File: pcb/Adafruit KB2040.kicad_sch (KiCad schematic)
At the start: 12 parts, among them M1 Vibrating-Motor, SW1 SW_SPST, U1 kb2040, U2 2465

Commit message: I messed around with the wiring more - now it should be done. need to do some final checks before sent off (whatever that means)
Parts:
- removed M1: Vibrating-Motor, Connector_PinHeader_2.54mm:PinHeader_1x02_P2.54mm_Vertical, symbol Motor:Motor_DC
- removed SW1: SW_SPST, Connector_PinHeader_2.54mm:PinHeader_1x02_P2.54mm_Vertical, symbol Switch:SW_SPST
- added ENPOINT1, GNDPOINT1: TestPoint_Small, TestPoint:TestPoint_Pad_2.0x2.0mm, symbol Connector:TestPoint_Small
- OLED1: footprint Connector_PinHeader_2.00mm:PinHeader_1x04_P2.00mm_Horizontal -> Connector_PinHeader_2.00mm:PinHeader_1x04_P2.00mm_Vertical
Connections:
- net D10ASSY: now also D-Pad1.4 (Center), U1.26 (D10); no longer D-Pad1.1 (Up), U1.10 (D6)
- net EN: now also ENPOINT1.1
- net GND: now also GNDPOINT1.1
- net at U1.9 (D5): no longer D-Pad1.4 (Center)
- new net D6ASSY: D-Pad1.1 (Up), U1.10 (D6)

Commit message: Maybe finished the board? looks good to me. gonna look it over with others first
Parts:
- added C2, C3, C4: 0.1uF, Capacitor_SMD:C_0201_0603Metric_Pad0.64x0.40mm_HandSolder, symbol Device:C_Small
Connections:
- net +3.3V: now also C2.1; no longer OLED1.2 (VCC)
- net +5V: now also C4.1
- net GND: now also C2.2, C4.2; no longer OLED1.1 (GND)

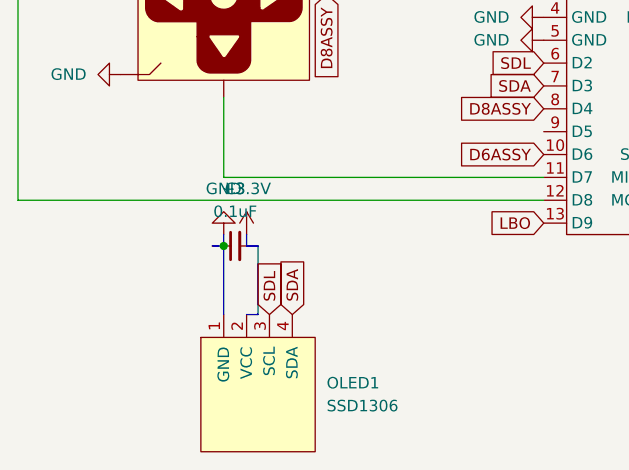
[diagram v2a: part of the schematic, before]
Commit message: Refreshed th eoled design to accomodate the screen i found - swapped vcc and gnd
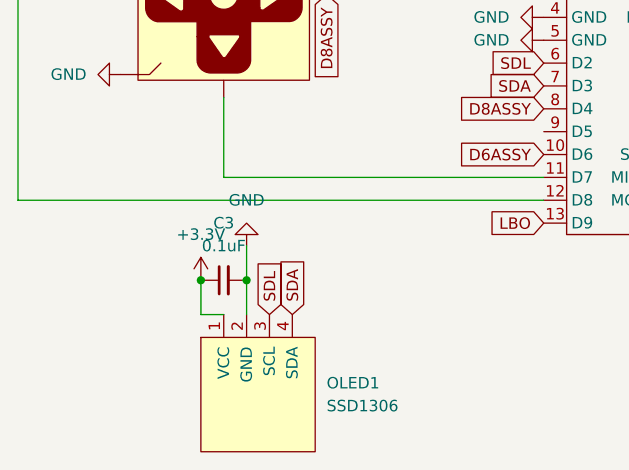
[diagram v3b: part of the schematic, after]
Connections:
- net +3.3V: now also C3.1, OLED1.1 (VCC)
- net GND: now also C3.2, OLED1.2 (GND)
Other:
- moved on the sheet: C3
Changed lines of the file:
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@@
 	(paper "A4")
 	(junction
-		(at 85.09 128.27)
+		(at 82.55 132.08)
 		(diameter 0)
 		(color 0 0 0 0)
@@
 	)
 	(junction
+		(at 87.63 132.08)
+		(diameter 0)
+		(color 0 0 0 0)
+	)
+	(junction
 		(at 142.24 105.41)
 		(diameter 0)
@@
 		)
 	)
-	(bus
-		(pts
-			(xy 87.63 128.27) (xy 88.9 128.27)
-		)
-		(stroke
-			(width 0)
-			(type default)
-		)
-	)
 	(wire
 		(pts
@@
 		)
 	)
-	(bus
-		(pts
-			(xy 85.09 127) (xy 85.09 128.27)
-		)
-		(stroke
-			(width 0)
-			(type default)
-		)
-	)
 	(wire
 		(pts
@@
 	(wire
 		(pts
-			(xy 189.23 102.87) (xy 190.5 102.87)
+			(xy 87.63 132.08) (xy 87.63 135.89)
 		)
 		(stroke
@@
 	(wire
 		(pts
-			(xy 209.55 102.87) (xy 198.12 102.87)
+			(xy 189.23 102.87) (xy 190.5 102.87)
 		)
 		(stroke
@@
 	(wire
 		(pts
-			(xy 100.33 91.44) (xy 96.52 91.44)
+			(xy 209.55 102.87) (xy 198.12 102.87)
 		)
 		(stroke
@@
 	(wire
 		(pts
-			(xy 120.65 123.19) (xy 62.23 123.19)
+			(xy 100.33 91.44) (xy 96.52 91.44)
 		)
 		(stroke
@@
 	(wire
 		(pts
-			(xy 147.32 97.79) (xy 147.32 85.09)
-		)
-		(stroke
-			(width 0)
-			(type default)
-		)
-	)
-	(bus
-		(pts
-			(xy 83.82 128.27) (xy 85.09 128.27)
+			(xy 120.65 123.19) (xy 62.23 123.19)
 		)
 		(stroke
@@
 		)
 	)
-	(bus
+	(wire
 		(pts
-			(xy 87.63 127) (xy 87.63 128.27)
+			(xy 147.32 97.79) (xy 147.32 85.09)
 		)
 		(stroke
@@
 		)
 	)
-	(bus
+	(wire
 		(pts
-			(xy 87.63 135.89) (xy 88.9 135.89)
+			(xy 82.55 135.89) (xy 82.55 132.08)
 		)
 		(stroke
@@
 		)
 	)
-	(bus
+	(wire
 		(pts
-			(xy 85.09 128.27) (xy 85.09 135.89)
+			(xy 162.56 85.09) (xy 162.56 91.44)
 		)
 		(stroke
@@
 	(wire
 		(pts
-			(xy 162.56 85.09) (xy 162.56 91.44)
+			(xy 209.55 77.47) (xy 209.55 102.87)
 		)
 		(stroke
@@
 	(wire
 		(pts
-			(xy 209.55 77.47) (xy 209.55 102.87)
+			(xy 85.09 135.89) (xy 82.55 135.89)
 		)
 		(stroke
@@
 		)
 	)
-	(bus
+	(wire
 		(pts
-			(xy 88.9 128.27) (xy 88.9 135.89)
+			(xy 120.65 120.65) (xy 85.09 120.65)
 		)
 		(stroke
@@
 	(wire
 		(pts
-			(xy 120.65 120.65) (xy 85.09 120.65)
+			(xy 99.06 49.53) (xy 113.03 49.53)
 		)
 		(stroke
@@
 	(wire
 		(pts
-			(xy 99.06 49.53) (xy 113.03 49.53)
+			(xy 187.96 102.87) (xy 189.23 102.87)
 		)
 		(stroke
@@
 	(wire
 		(pts
-			(xy 187.96 102.87) (xy 189.23 102.87)
+			(xy 87.63 128.27) (xy 87.63 132.08)
 		)
 		(stroke
@@
 	(symbol
 		(lib_id "power:+3.3V")
-		(at 87.63 127 0)
+		(at 82.55 132.08 0)
 		(unit 1)
 		(exclude_from_sim no)
@@
 		(fields_autoplaced yes)
 		(property "Reference" "#PWR05"
-			(at 87.63 130.81 0)
+			(at 82.55 135.89 0)
 			(effects
 				(font
@@
 		)
 		(property "Value" "+3.3V"
-			(at 87.63 121.92 0)
+			(at 82.55 127 0)
 			(effects
 				(font
@@
 		)
 		(property "Footprint" ""
-			(at 87.63 127 0)
+			(at 82.55 132.08 0)
 			(effects
 				(font
@@
 		)
 		(property "Datasheet" ""
-			(at 87.63 127 0)
+			(at 82.55 132.08 0)
 			(effects
 				(font
@@
 		)
 		(property "Description" "Power symbol creates a global label with name \"+3.3V\""
-			(at 87.63 127 0)
+			(at 82.55 132.08 0)
 			(effects
 				(font
@@
 	(symbol
 		(lib_id "Device:C_Small")
-		(at 86.36 128.27 90)
+		(at 85.09 132.08 90)
 		(unit 1)
 		(exclude_from_sim no)
@@
 		(fields_autoplaced yes)
 		(property "Reference" "C3"
-			(at 86.3663 121.92 90)
+			(at 85.0963 125.73 90)
 			(effects
 				(font
@@
 		)
 		(property "Value" "0.1uF"
-			(at 86.3663 124.46 90)
+			(at 85.0963 128.27 90)
 			(effects
 				(font
@@
 		)
 		(property "Footprint" "Capacitor_SMD:C_0201_0603Metric_Pad0.64x0.40mm_HandSolder"
-			(at 86.36 128.27 0)
+			(at 85.09 132.08 0)
 			(effects
 				(font
@@
 		)
 		(property "Datasheet" "~"
-			(at 86.36 128.27 0)
+			(at 85.09 132.08 0)
 			(effects
 				(font
@@
 		)
 		(property "Description" "Unpolarized capacitor, small symbol"
-			(at 86.36 128.27 0)
+			(at 85.09 132.08 0)
 			(effects
 				(font
@@
 	(symbol
 		(lib_id "power:GND")
-		(at 85.09 127 180)
+		(at 87.63 128.27 180)
 		(unit 1)
 		(exclude_from_sim no)
@@
 		(fields_autoplaced yes)
 		(property "Reference" "#PWR06"
-			(at 85.09 120.65 0)
+			(at 87.63 121.92 0)
 			(effects
 				(font
@@
 		)
 		(property "Value" "GND"
-			(at 85.09 121.92 0)
+			(at 87.63 123.19 0)
 			(effects
 				(font
@@
 		)
 		(property "Footprint" ""
-			(at 85.09 127 0)
+			(at 87.63 128.27 0)
 			(effects
 				(font
@@
 		)
 		(property "Datasheet" ""
-			(at 85.09 127 0)
+			(at 87.63 128.27 0)
 			(effects
 				(font
@@
 		)
 		(property "Description" "Power symbol creates a global label with name \"GND\" , ground"
-			(at 85.09 127 0)
+			(at 87.63 128.27 0)
 			(effects
 				(font
